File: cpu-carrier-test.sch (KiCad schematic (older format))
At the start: 26 parts, among them SW1 SW_Push

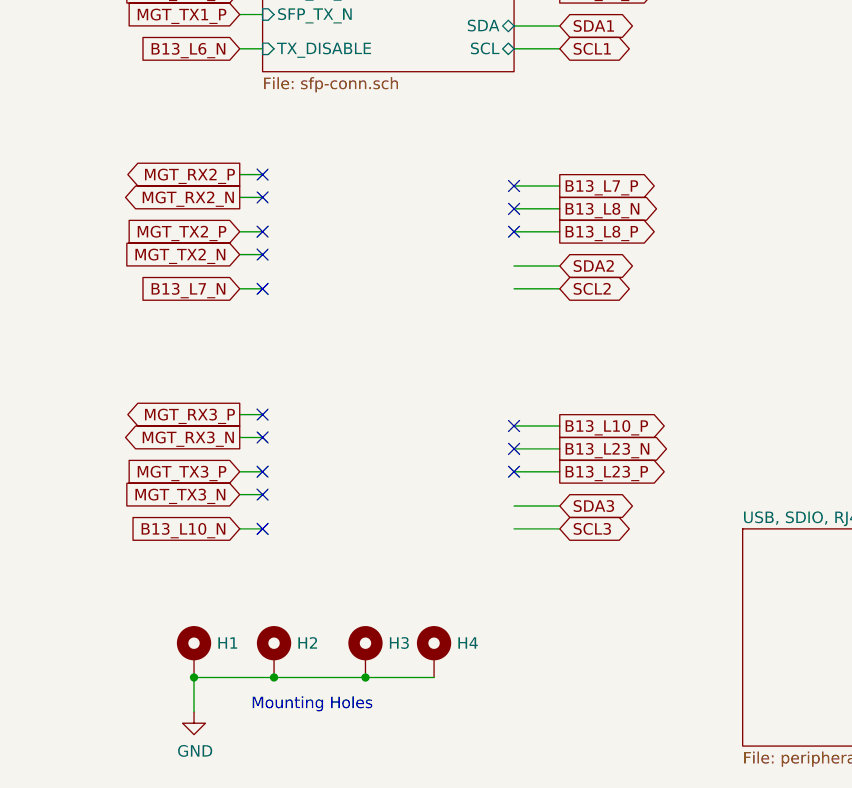
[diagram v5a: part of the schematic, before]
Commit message: re-routed usbA (proper diff-pair); added mounting holes
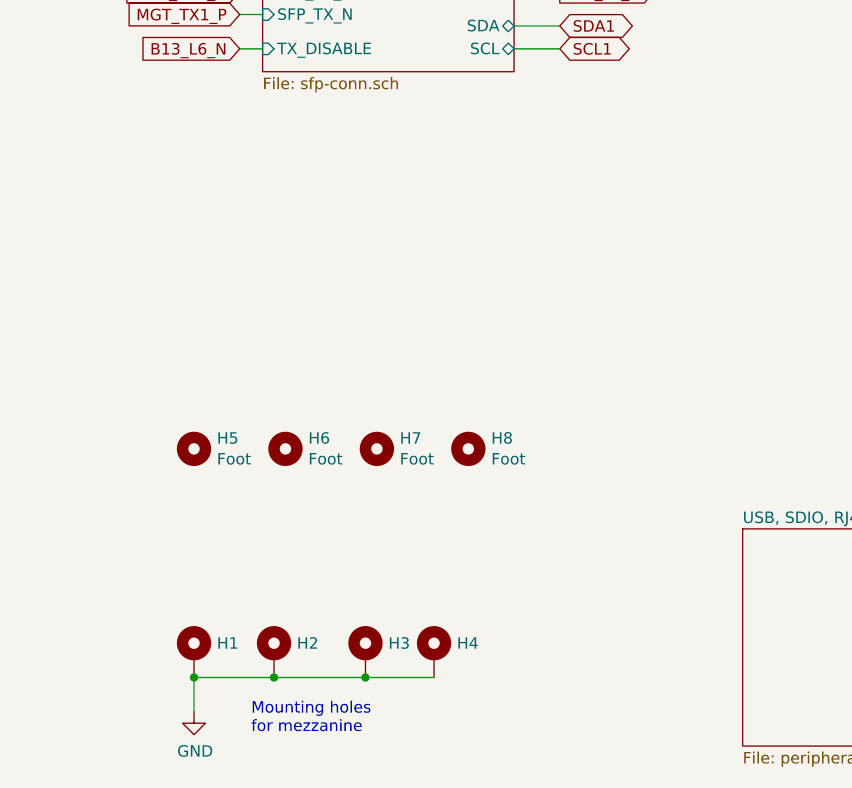
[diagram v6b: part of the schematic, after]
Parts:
- added H5, H6, H7, H8: Foot, proj_footprints:foot_ff-13, symbol Mechanical:MountingHole
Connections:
- no-connect marks 16 -> 0
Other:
- note added: "Mounting holes\nfor mezzanine"
- note removed: "Mounting Holes"
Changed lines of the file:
@@
 Wire Wire Line
 	1550 4550 1650 4550
-Wire Wire Line
-	2750 5650 2950 5650
-Wire Wire Line
-	2750 5750 2950 5750
-Text GLabel 1550 5350 0    50   Output ~ 0
-MGT_RX2_N
-Text GLabel 1550 5250 0    50   Output ~ 0
-MGT_RX2_P
-Text GLabel 1550 5500 0    50   Input ~ 0
-MGT_TX2_P
-Text GLabel 1550 5600 0    50   Input ~ 0
-MGT_TX2_N
-Wire Wire Line
-	1550 5250 1650 5250
-Wire Wire Line
-	1550 5350 1650 5350
-Wire Wire Line
-	1550 5500 1650 5500
-Wire Wire Line
-	1550 5600 1650 5600
-Wire Wire Line
-	2750 6700 2950 6700
-Wire Wire Line
-	2750 6800 2950 6800
-Text GLabel 1550 6400 0    50   Output ~ 0
-MGT_RX3_N
-Text GLabel 1550 6300 0    50   Output ~ 0
-MGT_RX3_P
-Text GLabel 1550 6550 0    50   Input ~ 0
-MGT_TX3_P
-Text GLabel 1550 6650 0    50   Input ~ 0
-MGT_TX3_N
-Wire Wire Line
-	1550 6300 1650 6300
-Wire Wire Line
-	1550 6400 1650 6400
-Wire Wire Line
-	1550 6550 1650 6550
-Wire Wire Line
-	1550 6650 1650 6650
 $Comp
 L power:GND #PWR?
@@
 Text GLabel 2950 4350 2    50   Output ~ 0
 B13_L4_N
-Text GLabel 2950 5300 2    50   Output ~ 0
-B13_L7_P
-Text GLabel 1550 5750 0    50   Input ~ 0
-B13_L7_N
-Text GLabel 2950 5500 2    50   Output ~ 0
-B13_L8_P
-Text GLabel 2950 5400 2    50   Output ~ 0
-B13_L8_N
-Text GLabel 2950 6350 2    50   Output ~ 0
-B13_L10_P
-Text GLabel 1550 6800 0    50   Input ~ 0
-B13_L10_N
-Text GLabel 2950 6550 2    50   Output ~ 0
-B13_L23_P
-Text GLabel 2950 6450 2    50   Output ~ 0
-B13_L23_N
 Wire Wire Line
 	2750 4250 2950 4250
@@
 Wire Wire Line
 	1550 4700 1650 4700
-Wire Wire Line
-	1550 5750 1650 5750
-Wire Wire Line
-	2750 5300 2950 5300
-Wire Wire Line
-	2750 5400 2950 5400
-Wire Wire Line
-	2750 5500 2950 5500
-Wire Wire Line
-	1550 6800 1650 6800
-Wire Wire Line
-	2750 6550 2950 6550
-Wire Wire Line
-	2750 6450 2950 6450
-Wire Wire Line
-	2750 6350 2950 6350
-Text GLabel 2950 6800 2    50   BiDi ~ 0
-SCL3
-Text GLabel 2950 6700 2    50   BiDi ~ 0
-SDA3
-Text GLabel 2950 5750 2    50   BiDi ~ 0
-SCL2
-Text GLabel 2950 5650 2    50   BiDi ~ 0
-SDA2
 Text GLabel 2950 4600 2    50   BiDi ~ 0
 SDA1
@@
 	1    0    0    -1
 $EndComp
-NoConn ~ 1650 5250
-NoConn ~ 1650 5350
-NoConn ~ 1650 5500
-NoConn ~ 1650 5600
-NoConn ~ 1650 5750
-NoConn ~ 1650 6300
-NoConn ~ 1650 6400
-NoConn ~ 1650 6550
-NoConn ~ 1650 6650
-NoConn ~ 1650 6800
-NoConn ~ 2750 6350
-NoConn ~ 2750 6450
-NoConn ~ 2750 6550
-NoConn ~ 2750 5500
-NoConn ~ 2750 5400
-NoConn ~ 2750 5300
 Wire Wire Line
 	4450 2550 4600 2550
@@
 Text Notes 5750 3550 0    50   ~ 0
 GREEN LED
-Text Notes 1600 7600 0    50   ~ 0
-Mounting Holes
+Text Notes 1600 7700 0    50   ~ 0
+Mounting holes\nfor mezzanine
 $Comp
 L Device:R_Small R?
@@
 Text GLabel 4700 6100 0    50   Input ~ 0
 B13_L18_P
+$Comp
+L Mechanical:MountingHole H5
+U 1 1 60EE52C3
+P 1350 6450
+F 0 "H5" H 1450 6496 50  0000 L CNN
+F 1 "Foot" H 1450 6405 50  0000 L CNN
+F 2 "proj_footprints:foot_ff-13" H 1350 6450 50  0001 C CNN
+F 3 "~" H 1350 6450 50  0001 C CNN
+	1    1350 6450
+	1    0    0    -1
+$EndComp
+$Comp
+L Mechanical:MountingHole H6
+U 1 1 60EE550C
+P 1750 6450
+F 0 "H6" H 1850 6496 50  0000 L CNN
+F 1 "Foot" H 1850 6405 50  0000 L CNN
+F 2 "proj_footprints:foot_ff-13" H 1750 6450 50  0001 C CNN
+F 3 "~" H 1750 6450 50  0001 C CNN
+	1    1750 6450
+	1    0    0    -1
+$EndComp
+$Comp
+L Mechanical:MountingHole H7
+U 1 1 60EE5653
+P 2150 6450
+F 0 "H7" H 2250 6496 50  0000 L CNN
+F 1 "Foot" H 2250 6405 50  0000 L CNN
+F 2 "proj_footprints:foot_ff-13" H 2150 6450 50  0001 C CNN
+F 3 "~" H 2150 6450 50  0001 C CNN
+	1    2150 6450
+	1    0    0    -1
+$EndComp
+$Comp
+L Mechanical:MountingHole H8
+U 1 1 60EE5954
+P 2550 6450
+F 0 "H8" H 2650 6496 50  0000 L CNN
+F 1 "Foot" H 2650 6405 50  0000 L CNN
+F 2 "proj_footprints:foot_ff-13" H 2550 6450 50  0001 C CNN
+F 3 "~" H 2550 6450 50  0001 C CNN
+	1    2550 6450
+	1    0    0    -1
+$EndComp
 $EndSCHEMATC
